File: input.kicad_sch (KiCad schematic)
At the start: 8 parts

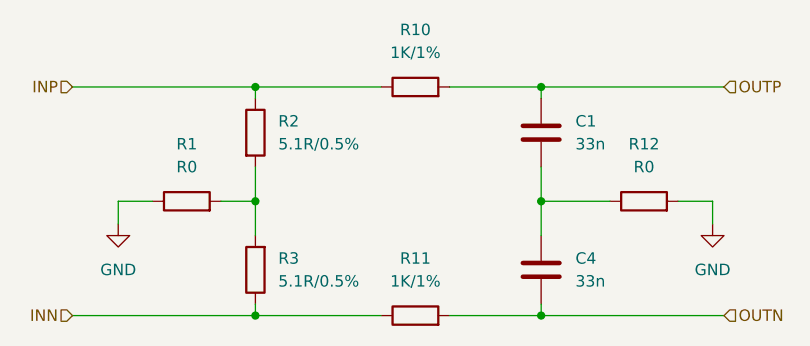
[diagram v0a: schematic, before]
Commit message: Change connector, assign JLCPCB
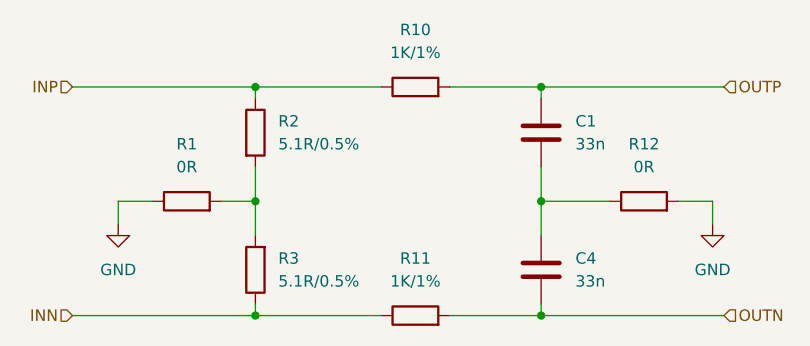
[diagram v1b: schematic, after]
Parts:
- C1, C4: LCSC (none) -> C21117
- R1, R12: value R0 -> 0R; LCSC (none) -> C21189
- R10, R11: LCSC (none) -> C21190
- R2, R3: LCSC (none) -> C25197
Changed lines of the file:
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@@
 			)
 		)
-		(property "Datasheet" "~"
+		(property "Datasheet" "https://wmsc.lcsc.com/wmsc/upload/file/pdf/v2/lcsc/2205311845_UNI-ROYAL-Uniroyal-Elec-0603WAF510KT5E_C25197.pdf"
 			(at 96.52 93.98 0)
 			(effects
@@
 		)
 		(property "Description" "Resistor"
+			(at 96.52 93.98 0)
+			(effects
+				(font
+					(size 1.27 1.27)
+				)
+				(hide yes)
+			)
+		)
+		(property "LCSC" "C25197"
 			(at 96.52 93.98 0)
 			(effects
@@
 			)
 		)
-		(property "Datasheet" "~"
+		(property "Datasheet" "https://wmsc.lcsc.com/wmsc/upload/file/pdf/v2/lcsc/2206010130_UNI-ROYAL-Uniroyal-Elec-0603WAF1001T5E_C21190.pdf"
 			(at 114.3 99.06 0)
 			(effects
@@
 		)
 		(property "Description" "Resistor"
+			(at 114.3 99.06 0)
+			(effects
+				(font
+					(size 1.27 1.27)
+				)
+				(hide yes)
+			)
+		)
+		(property "LCSC" "C21190"
 			(at 114.3 99.06 0)
 			(effects
@@
 			)
 		)
-		(property "Datasheet" "~"
+		(property "Datasheet" "https://wmsc.lcsc.com/wmsc/upload/file/pdf/v2/lcsc/2205311845_UNI-ROYAL-Uniroyal-Elec-0603WAF510KT5E_C25197.pdf"
 			(at 96.52 78.74 0)
 			(effects
@@
 		)
 		(property "Description" "Resistor"
+			(at 96.52 78.74 0)
+			(effects
+				(font
+					(size 1.27 1.27)
+				)
+				(hide yes)
+			)
+		)
+		(property "LCSC" "C25197"
 			(at 96.52 78.74 0)
 			(effects
@@
 			)
 		)
-		(property "Value" "R0"
+		(property "Value" "0R"
 			(at 88.9 82.55 90)
 			(effects
@@
 			)
 		)
-		(property "Datasheet" "~"
+		(property "Datasheet" "https://wmsc.lcsc.com/wmsc/upload/file/pdf/v2/lcsc/2206010130_UNI-ROYAL-Uniroyal-Elec-0603WAF0000T5E_C21189.pdf"
 			(at 88.9 86.36 0)
 			(effects
@@
 		)
 		(property "Description" "Resistor"
+			(at 88.9 86.36 0)
+			(effects
+				(font
+					(size 1.27 1.27)
+				)
+				(hide yes)
+			)
+		)
+		(property "LCSC" "C21189"
 			(at 88.9 86.36 0)
 			(effects
@@
 			)
 		)
-		(property "Datasheet" "~"
+		(property "Datasheet" "https://wmsc.lcsc.com/wmsc/upload/file/pdf/v2/lcsc/2304140030_Samsung-Electro-Mechanics-CL10B333KB8NNNC_C21117.pdf"
 			(at 128.27 93.98 0)
 			(effects
@@
 		)
 		(property "Description" "Unpolarized capacitor"
+			(at 128.27 93.98 0)
+			(effects
+				(font
+					(size 1.27 1.27)
+				)
+				(hide yes)
+			)
+		)
+		(property "LCSC" "C21117"
 			(at 128.27 93.98 0)
 			(effects
@@
 			)
 		)
-		(property "Datasheet" "~"
+		(property "Datasheet" "https://wmsc.lcsc.com/wmsc/upload/file/pdf/v2/lcsc/2206010130_UNI-ROYAL-Uniroyal-Elec-0603WAF1001T5E_C21190.pdf"
 			(at 114.3 73.66 0)
 			(effects
@@
 		)
 		(property "Description" "Resistor"
+			(at 114.3 73.66 0)
+			(effects
+				(font
+					(size 1.27 1.27)
+				)
+				(hide yes)
+			)
+		)
+		(property "LCSC" "C21190"
 			(at 114.3 73.66 0)
 			(effects
@@
 			)
 		)
-		(property "Value" "R0"
+		(property "Value" "0R"
 			(at 139.7 82.55 90)
 			(effects
@@
 			)
 		)
-		(property "Datasheet" "~"
+		(property "Datasheet" "https://wmsc.lcsc.com/wmsc/upload/file/pdf/v2/lcsc/2206010130_UNI-ROYAL-Uniroyal-Elec-0603WAF0000T5E_C21189.pdf"
 			(at 139.7 86.36 0)
 			(effects
@@
 		)
 		(property "Description" "Resistor"
+			(at 139.7 86.36 0)
+			(effects
+				(font
+					(size 1.27 1.27)
+				)
+				(hide yes)
+			)
+		)
+		(property "LCSC" "C21189"
 			(at 139.7 86.36 0)
 			(effects
@@
 			)
 		)
-		(property "Datasheet" "~"
+		(property "Datasheet" "https://wmsc.lcsc.com/wmsc/upload/file/pdf/v2/lcsc/2304140030_Samsung-Electro-Mechanics-CL10B333KB8NNNC_C21117.pdf"
 			(at 128.27 78.74 0)
 			(effects
@@
 			(at 128.27 78.74 0)
 			(effects
+				(font
+					(size 1.27 1.27)
+				)
+				(hide yes)
+			)
+		)
+		(property "LCSC" "C21117"
+			(at 128.27 78.74 0)
+			(effects

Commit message: First order
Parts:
- R2, R3: LCSC C25197 -> C657209
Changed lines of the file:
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@@
 			)
 		)
-		(property "Datasheet" "https://wmsc.lcsc.com/wmsc/upload/file/pdf/v2/lcsc/2205311845_UNI-ROYAL-Uniroyal-Elec-0603WAF510KT5E_C25197.pdf"
+		(property "Datasheet" "https://wmsc.lcsc.com/wmsc/upload/file/pdf/v2/lcsc/2304140030_FH--Guangdong-Fenghua-Advanced-Tech-TD03G5R10BT_C657209.pdf"
 			(at 96.52 93.98 0)
 			(effects
@@
 			)
 		)
-		(property "LCSC" "C25197"
+		(property "LCSC" "C657209"
 			(at 96.52 93.98 0)
 			(effects
@@
 			)
 		)
-		(property "Datasheet" "https://wmsc.lcsc.com/wmsc/upload/file/pdf/v2/lcsc/2205311845_UNI-ROYAL-Uniroyal-Elec-0603WAF510KT5E_C25197.pdf"
+		(property "Datasheet" "https://wmsc.lcsc.com/wmsc/upload/file/pdf/v2/lcsc/2304140030_FH--Guangdong-Fenghua-Advanced-Tech-TD03G5R10BT_C657209.pdf"
 			(at 96.52 78.74 0)
 			(effects
@@
 			)
 		)
-		(property "LCSC" "C25197"
+		(property "LCSC" "C657209"
 			(at 96.52 78.74 0)
 			(effects
